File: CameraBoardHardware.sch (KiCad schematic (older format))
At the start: 25 parts

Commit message: switched to TI parts, still need to create rca/barrel jack
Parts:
- removed C?: 10uf, symbol C
- removed D?: LED, symbol LED
- removed J?: Video_Out, symbol Conn_Coaxial
- removed R? (x3): 500, symbol R
- removed R? (x2): 75, symbol R
- removed R? (x2): R, symbol R
- removed U?: TM4C129E_Launchpad_X7, symbol TM4C129E_Launchpad_X7
- removed U?: MAX4311EEE+, 21-0055H_16, symbol MAX4311EEE+
- removed U?: Camera4, symbol Molex_SL_3
- removed U?: Camera3, symbol Molex_SL_3
- removed U?: Camera1, symbol Molex_SL_3
- removed U?: Camera2, symbol Molex_SL_3
- added C?: Anderson_3, symbol Anderson_3
- added C? (x10): 10uf, symbol C
- added C? (x2): 0.1uf, symbol C
- added D?: LED, symbol LED
- added J?: CON4-B579X575R_COAXP, CON4-B579X575R_COAXP, symbol CON4-B579X575R_COAXP
- added R?: 100k, symbol R
- added R? (x2): 470, symbol R
- added R? (x4): 75, symbol R
- added R?: 330, symbol R
- added U?: TM4C129E_Launchpad_X7, symbol TM4C129E_Launchpad_X7
- added U?: LMH6574MA, M14A, symbol LMH6574MA
- added U?: TXB0102_DCU_8, DCU8, symbol TXB0102_DCU_8
- added U? (x4): Molex_SL_3, symbol Molex_SL_3
- added U? (x4): Picoblade_3, symbol Picoblade_3
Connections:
- net labels added: 12VA, 3.3V, A0, A1, A2, B1, B2, Camera1_In, Camera2_In, Camera3_In, Camera4_In, ETC..., OE, TODO_MAKE_12V_DC_BARREL_JACK_DEVICE, TODO_RCA_INPUT_DEVICE, Video_Out
- net labels removed: +12V, +12VA, +5V, 12V_Act, GND, digitalWrite_MuxA0, digitalWrite_MuxA1
- wire segments 54 -> 100
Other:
- moved on the sheet: C?, R?

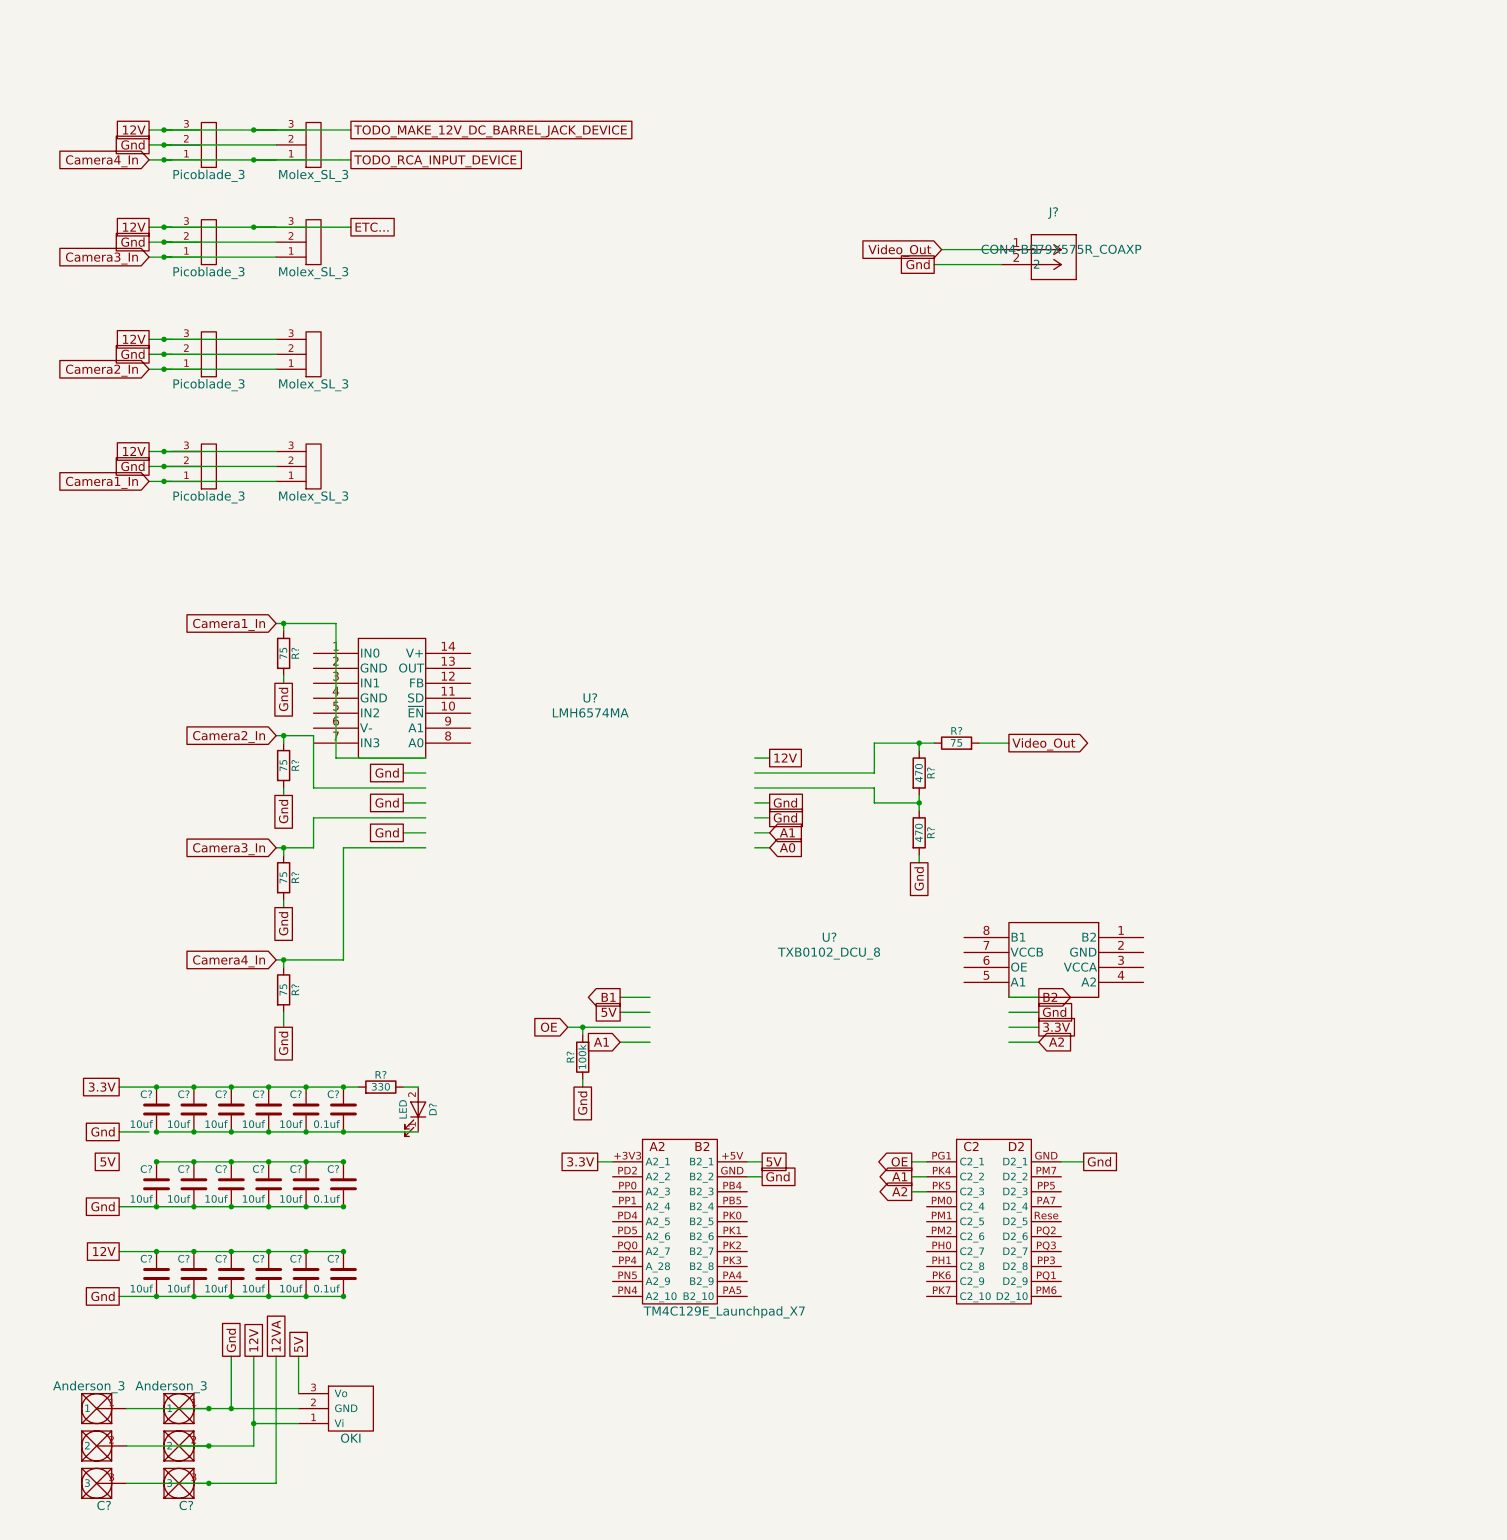
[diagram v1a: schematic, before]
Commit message: layout ready to run traces
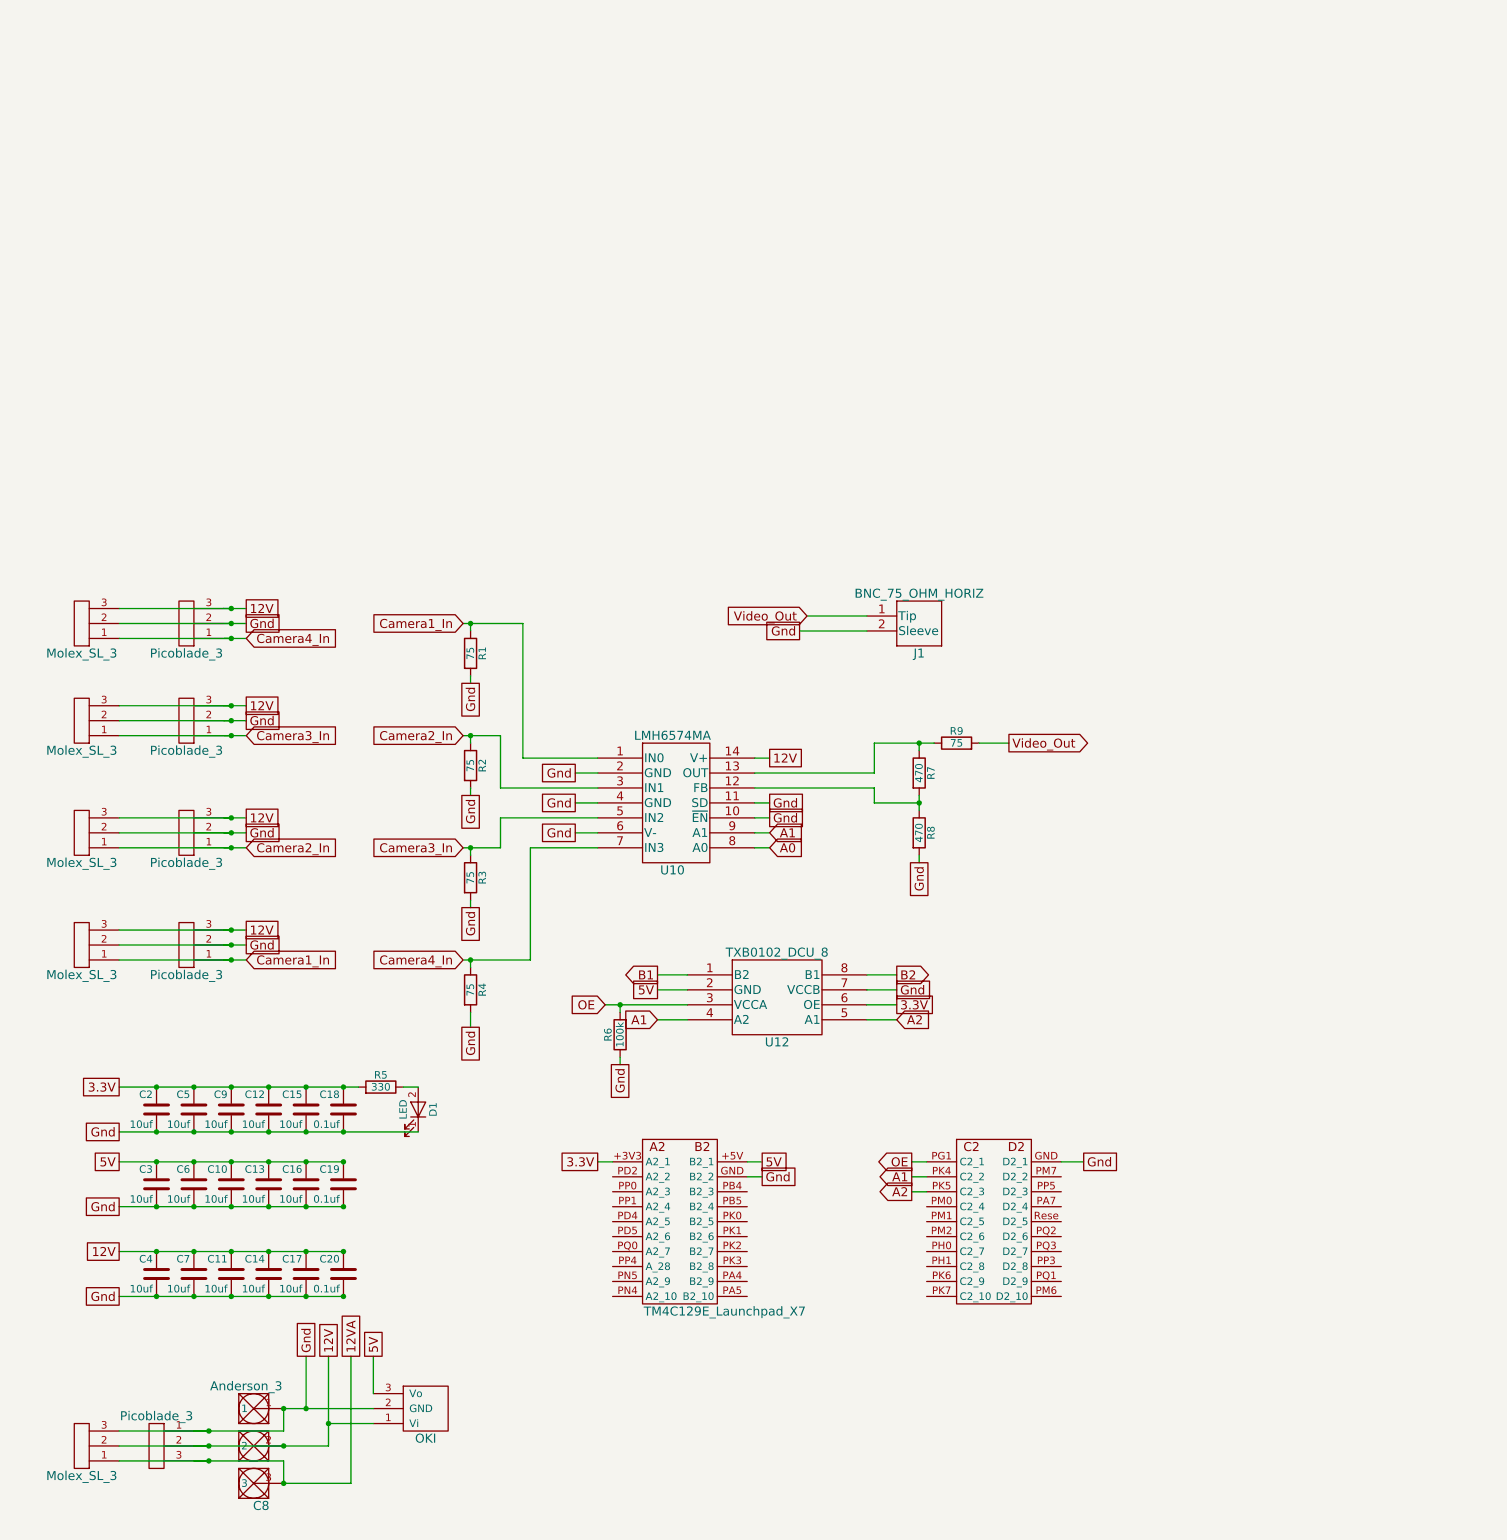
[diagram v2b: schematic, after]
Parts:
- removed C?: Anderson_3, symbol Anderson_3
- removed J?: CON4-B579X575R_COAXP, CON4-B579X575R_COAXP, symbol CON4-B579X575R_COAXP
- removed U?: LMH6574MA, M14A, symbol LMH6574MA
- removed U?: TXB0102_DCU_8, DCU8, symbol TXB0102_DCU_8
- added J1: BNC_75_OHM_HORIZ, BNC-75-Ohm-HORIZONTAL:BNC-75-Ohm-HORIZONTAL-1-1478032-0, symbol BNC_75_OHM_HORIZ
- added U10: LMH6574MA, LMH6574MANOPB:LMH6574MA&slash_NOPB, symbol LMH6574MA
- added U12: TXB0102_DCU_8, TXB0102DCUR:TXB0102DCUR, symbol TXB0102_DCU_8
- added U13: Molex_SL_3, MRDT_Connectors:MOLEX_SL_3_Horizontal, symbol Molex_SL_3
- added U14: Picoblade_3, Connectors_Molex:Molex_PicoBlade_53047-0310_03x1.25mm_Straight, symbol Picoblade_3
- C10, C11, C12, C13, C14, C15, C16, C17, C18, C19, C2, C20, C3, C4, C5, C6, C7, C9: renamed from C?; footprint (none) -> Capacitors_SMD:C_0603_HandSoldering
- C8: renamed from C?; footprint (none) -> MRDT_Connectors:Anderson_3_Horisontal_Side_by_Side
- D1: renamed from D?; footprint (none) -> LEDs:LED_0603_HandSoldering
- R1, R2, R3, R4, R5, R6, R7, R8, R9: renamed from R?; footprint (none) -> Resistors_SMD:R_0603_HandSoldering
- U1, U2, U3, U4: renamed from U?; footprint (none) -> Connectors_Molex:Molex_PicoBlade_53047-0310_03x1.25mm_Straight
- U11: renamed from U?; footprint (none) -> MRDT_Shields:TM4C129E_Launchpad_X7_Bottom_SMD
- U5, U6, U7, U8: renamed from U?; footprint (none) -> MRDT_Connectors:MOLEX_SL_3_Horizontal
- U9: renamed from U?; footprint (none) -> MRDT_Devices:OKI_Horisontal
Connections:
- net labels removed: ETC..., TODO_MAKE_12V_DC_BARREL_JACK_DEVICE, TODO_RCA_INPUT_DEVICE
- wire segments 100 -> 103
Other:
- moved on the sheet: C8, R1, R2, R3, R4, R6

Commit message: Gerbs
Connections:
- net A0 is gone; now on net B1: U10.8 (A0)
- net 3.3V: now also R6.2, U12.3 (VCCA); no longer U12.6 (OE)
- net 5V: now also U12.7 (VCCB); no longer U12.2 (GND)
- net A1: now also U12.5 (A1); no longer U10.9 (A1), U12.4 (A2)
- net A2: now also U12.4 (A2); no longer U12.5 (A1)
- net B1: now also U12.8 (B1); no longer U12.1 (B2)
- net B2: now also U10.9 (A1), U12.1 (B2); no longer U12.8 (B1)
- net Gnd: now also U12.2 (GND); no longer U12.7 (VCCB)
- net OE: now also U12.6 (OE); no longer R6.2, U12.3 (VCCA)
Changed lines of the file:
@@
 5V
 Text GLabel 4650 6750 0    60   UnSpc ~ 0
-5V
+Gnd
 $Comp
 L R R9
@@
 Wire Wire Line
 	7350 7900 7500 7900
-Text GLabel 6250 6750 2    60   UnSpc ~ 0
-Gnd
-Text GLabel 6250 6850 2    60   UnSpc ~ 0
-3.3V
+Text GLabel 6250 6750 2    60   Input ~ 0
+5V
+Text GLabel 6250 6850 2    60   Input ~ 0
+OE
 Connection ~ 2150 10050
 Wire Wire Line
@@
 $EndComp
 Text GLabel 4300 6850 0    60   Input ~ 0
-OE
+3.3V
 Text GLabel 4650 6950 0    60   Input ~ 0
+A2
+Text GLabel 4650 6650 0    60   Output ~ 0
+B2
+Text GLabel 6250 6650 2    60   Output ~ 0
+B1
+Text GLabel 6250 6950 2    60   Input ~ 0
 A1
-Text GLabel 4650 6650 0    60   Output ~ 0
-B1
-Text GLabel 6250 6650 2    60   Output ~ 0
-B2
-Text GLabel 6250 6950 2    60   Input ~ 0
-A2
 Wire Wire Line
 	6050 6650 6250 6650
@@
 $EndComp
 Text GLabel 5400 5700 2    60   Input ~ 0
-A1
+B2
 Text GLabel 5400 5800 2    60   Input ~ 0
-A0
+B1
 Wire Wire Line
 	5300 5700 5400 5700
